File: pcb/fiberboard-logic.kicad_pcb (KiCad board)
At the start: 2 copper layers, 172 x 98 mm, 59 parts, among them J1 VIN, J3 FOOT, J4 NPN, J5 RLY1, J6 RLY2, J7 SOL, J8 RS485, J9 OLED, K1 G6KU-2F-Y, K2 G6KU-2F-Y, Q12 AO4407A, Q3 2N3904, Q4 2N3904, Q5 AO3400A, U1 ESP32-DevKitC, U2 XL1509-5.0, U3 AMS1117-3.3, U5 PC817, U6 PC817, U7 MAX485E

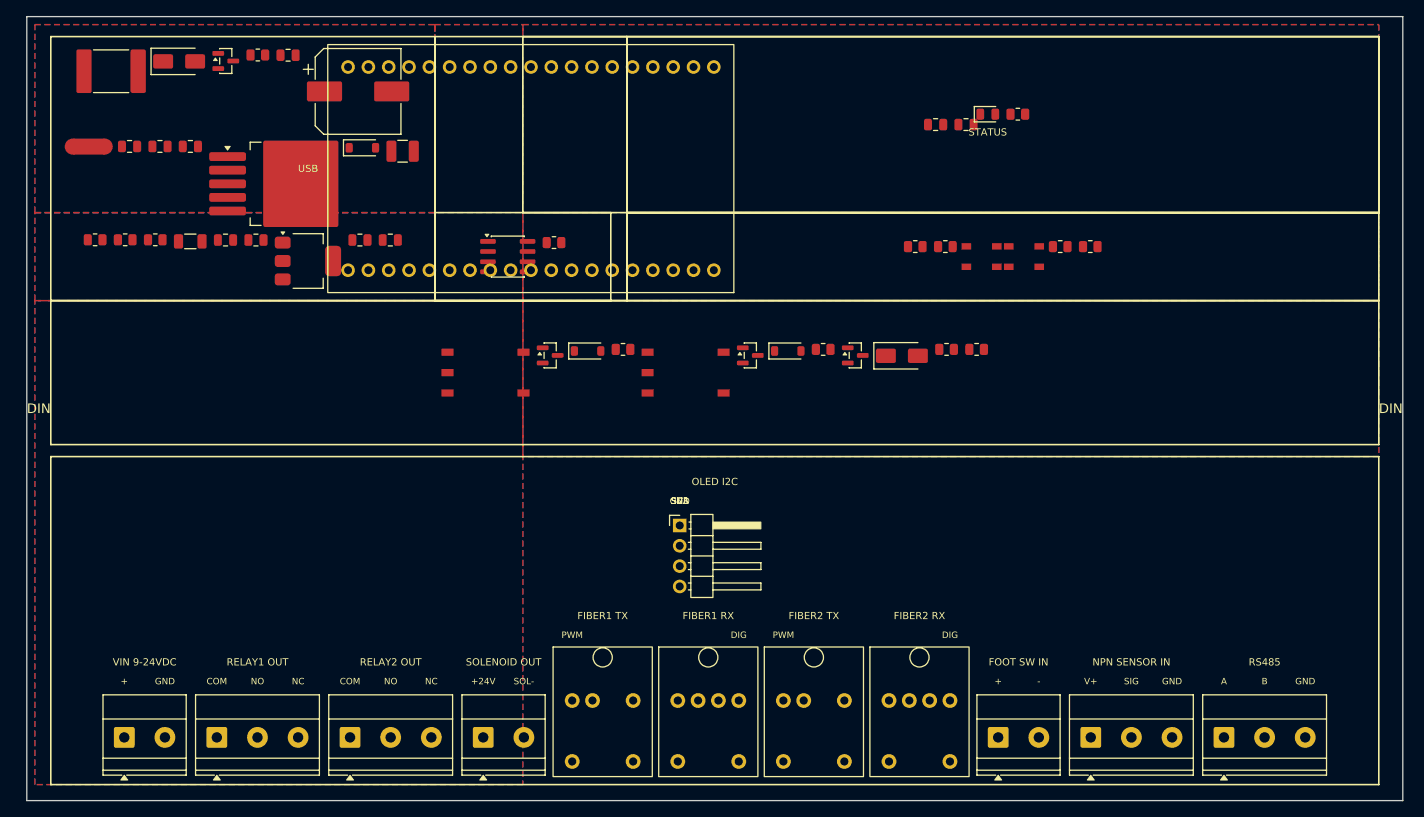
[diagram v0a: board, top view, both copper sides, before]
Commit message: thêm các linh kiện bảo vệ nguồn và sửa layout để lắp vào hộp PLC 45x90x40mm 2 hàng giắc
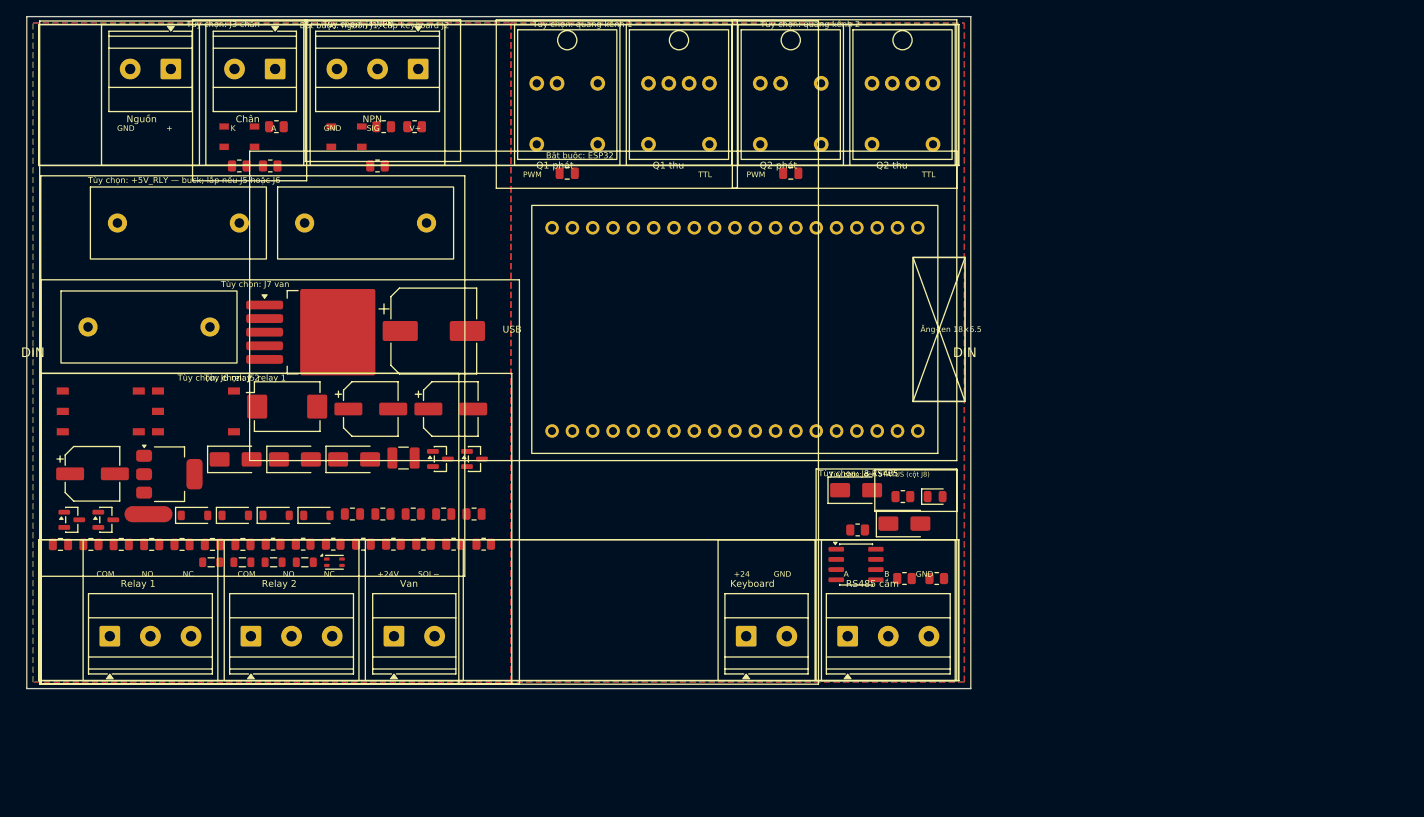
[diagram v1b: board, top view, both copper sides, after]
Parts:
- removed J9: OLED, Connector_PinHeader_2.54mm:PinHeader_1x04_P2.54mm_Horizontal
- added C19: 10uF, Capacitor_SMD:C_0805_2012Metric, F.Cu at (40.7, 62.2)
- added C21: 100nF, Capacitor_SMD:C_0805_2012Metric, F.Cu at (23.2, 66.0)
- added C22: 220uF, Capacitor_SMD:CP_Elec_6.3x5.4, F.Cu at (53.0, 49.0)
- added C23: 100nF, Capacitor_SMD:C_0805_2012Metric, F.Cu at (52.1, 62.2)
- added C24: 220uF, Capacitor_SMD:CP_Elec_6.3x5.4, F.Cu at (8.21, 57.1)
- added C25: 100nF, Capacitor_SMD:C_0805_2012Metric, F.Cu at (27.0, 66.0)
- added D10: SMAJ5.0A, Diode_SMD:D_SMA, F.Cu at (103.7, 59.2)
- added D11: SMAJ5.0A, Diode_SMD:D_SMA, F.Cu at (33.5, 55.4)
- added D12: SMAJ5.0A, Diode_SMD:D_SMA, F.Cu at (40.9, 55.4)
- added D9: SMAJ5.0A, Diode_SMD:D_SMA, F.Cu at (109.7, 63.4)
- added F2: 5x20 F0.5A, Fiberboard:Fuseholder_5x20mm_Horizontal, F.Cu at (42.4, 25.8)
- added F3: 5x20 F0.25A, Fiberboard:Fuseholder_5x20mm_Horizontal, F.Cu at (15.3, 38.8)
- added FB1: BLM21PG121, Inductor_SMD:L_0805_2012Metric, F.Cu at (30.9, 68.2)
- added FB2: BLM21PG121, Inductor_SMD:L_0805_2012Metric, F.Cu at (26.9, 68.2)
- added FB3: BLM21PG121, Inductor_SMD:L_0805_2012Metric, F.Cu at (23.1, 68.2)
- added FB4: BLM21PG121, Inductor_SMD:L_0805_2012Metric, F.Cu at (34.8, 68.2)
- added J2: KB24, Fiberboard:Terminal_2EDG5.08-1x02_P5.08mm_Horizontal, F.Cu at (89.9, 77.5)
- added L2: ACM2012, Inductor_SMD:L_CommonModeChoke_Coilank_ACM2012, F.Cu at (38.5, 68.2)
- added R18: 10R, Resistor_SMD:R_0805_2012Metric, F.Cu at (113.7, 70.2)
- added R19: 10R, Resistor_SMD:R_0805_2012Metric, F.Cu at (103.9, 64.2)
- added R20: 100k, Resistor_SMD:R_0805_2012Metric, F.Cu at (30.4, 18.7)
- added R21: 100k, Resistor_SMD:R_0805_2012Metric, F.Cu at (43.8, 18.7)
- added RV1: MOV-26V, Varistor:Varistor_Panasonic_VF, F.Cu at (32.5, 48.8)
- C2: value 100uF -> 220uF; footprint Capacitor_SMD:C_1206_3216Metric -> Capacitor_SMD:CP_Elec_6.3x5.4
- C4: value 470uF -> 1000uF; footprint Capacitor_SMD:CP_Elec_10x10.5 -> Capacitor_SMD:CP_Elec_10x12.5
- D3, D4: value 1N4148 -> SS34
- D5: footprint Diode_SMD:D_SMA -> Diode_SMD:D_SOD-123
- F1: value MF-MSMF350 -> 5x20 F4A; footprint Fuse:Fuse_2920_7451Metric -> Fiberboard:Fuseholder_5x20mm_Horizontal
- J1, J3, J7: footprint TerminalBlock_Phoenix:TerminalBlock_Phoenix_MKDS-1,5-2-5.08_1x02_P5.08mm_Horizontal -> Fiberboard:Terminal_2EDG5.08-1x02_P5.08mm_Horizontal
- J4, J5, J6: footprint TerminalBlock_Phoenix:TerminalBlock_Phoenix_MKDS-1,5-3-5.08_1x03_P5.08mm_Horizontal -> Fiberboard:Terminal_2EDG5.08-1x03_P5.08mm_Horizontal
- J8: value RS485 -> RS485-2EDG3P; footprint TerminalBlock_Phoenix:TerminalBlock_Phoenix_MKDS-1,5-3-5.08_1x03_P5.08mm_Horizontal -> Fiberboard:Terminal_2EDG5.08-1x03_P5.08mm_Horizontal
- R13: value 100R -> 100
- R15: value 120R -> 100
- U1: value ESP32-DevKitC -> ESP32-DevKitC-32E
- moved J3 123.1 mm to (31.0, 6.55), turned to 180 degrees
- moved J4 118.5 mm to (48.9, 6.55), turned to 180 degrees
- moved R9 103.1 mm to (26.6, 18.7)
- moved Q5 95.9 mm to (9.88, 62.9)
- moved U5 94.0 mm to (26.6, 15.0)
- moved Q4 87.3 mm to (5.62, 62.9)
- moved U6 86.0 mm to (40.0, 15.0)
- moved R10 85.8 mm to (48.5, 13.8)
- moved J1 83.8 mm to (18.0, 6.55), turned to 180 degrees
- moved R7 81.2 mm to (31.2, 13.8)
- moved F1T 77.3 mm to (67.6, 12.2)
- moved F1R 77.2 mm to (81.5, 12.2)
- moved F2T 77.2 mm to (95.5, 12.2)
- moved F2R 77.2 mm to (109.5, 12.2)
- moved D5 75.8 mm to (36.3, 62.4)
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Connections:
- C18 pad 1: +3V3 -> +3V3_REG
- C2 pad 1: +5V -> +5V_RAW
- C3 pad 1: +3V3 -> +3V3_REG
- C5 pad 1: +5V -> +5V_RAW
- D3 pad 1: +5V -> +5V_RLY
- D4 pad 1: +5V -> +5V_RLY
- D5 pad 1: +24V -> +24V_SOL
- F1 pad 2: VIN_FUSE -> VIN_CM_IN
- J1 pad 2: GND_PWR -> VIN_CM_RET
- J7 pad 1: +24V -> +24V_SOL
- J8 pad 1: RS485_A -> RS485_A_BUS
- J8 pad 2: RS485_B -> RS485_B_BUS
- K1 pad 1: +5V -> +5V_RLY
- K2 pad 1: +5V -> +5V_RLY
- L1 pad 2: +5V -> +5V_RAW
- NT1 pad 2: GND -> GND_SPLICE
- R15 pad 1: RS485_A -> RS485_A_BUS
- R15 pad 2: RS485_B -> RS485_B_BUS
- U1 pad 13: GND -> (no net)
- U1 pad 14: (no net) -> GND
- U3 pad 2: +3V3 -> +3V3_REG
- U6 pad 2: GND -> GND_PWR
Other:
- board size 172 x 98 mm -> 118 x 84 mm
- board text added: "+24"
- board text added: "Bắt buộc: ESP32"
- board text added: "Bắt buộc: nguồn J1, cấp keyboard J2"
- board text added: "Chân"
- board text added: "K"
- board text added: "Keyboard"
- board text added: "NPN"
- board text added: "Nguồn"
- board text added: "Q1 phát"
- board text added: "Q1 thu"
- board text added: "Q2 phát"
- board text added: "Q2 thu"
- board text added: "RS485 cắm"
- board text added: "Relay 1"
- board text added: "Relay 2"
- board text added: "SOL−"
- board text added: "TTL"
- board text added: "Tùy chọn: +5V_RLY — buck; lắp nếu J5 hoặc J6"
- board text added: "Tùy chọn: J3 chân"
- board text added: "Tùy chọn: J4 NPN"
- board text added: "Tùy chọn: J5 relay 1"
- board text added: "Tùy chọn: J6 relay 2"
- board text added: "Tùy chọn: J7 van"
- board text added: "Tùy chọn: J8 RS485"
- board text added: "Tùy chọn: quang kênh 1"
- board text added: "Tùy chọn: quang kênh 2"
- board text added: "Tùy chọn: đèn STATUS (cột J8)"
- board text added: "Van"
- board text added: "Ăng-ten 18×6.5"
- board text removed: "-"
- board text removed: "3V3"
- board text removed: "DIG"
- board text removed: "FIBER1 RX"
- board text removed: "FIBER1 TX"
- board text removed: "FIBER2 RX"
- board text removed: "FIBER2 TX"
- board text removed: "FOOT SW IN"
- board text removed: "NPN SENSOR IN"
- board text removed: "OLED I2C"
- board text removed: "RELAY1 OUT"
- board text removed: "RELAY2 OUT"
- board text removed: "RS485"
- board text removed: "SCL"
- board text removed: "SDA"
- board text removed: "SOL-"
- board text removed: "SOLENOID OUT"
- board text removed: "STATUS"
- board text removed: "VIN 9-24VDC"

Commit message: chia vùng linh kiện để sắp xếp và tránh linh kiện quá dày
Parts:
- removed F2: 5x20 F0.5A, Fiberboard:Fuseholder_5x20mm_Horizontal
- removed F3: 5x20 F0.25A, Fiberboard:Fuseholder_5x20mm_Horizontal
- added C26: 220uF, Capacitor_SMD:CP_Elec_6.3x5.4, F.Cu at (50.3, 67.7)
- added C27: 100nF, Capacitor_SMD:C_0805_2012Metric, F.Cu at (52.8, 62.2)
- added D13: VIN, LED_SMD:LED_0805_2012Metric, F.Cu at (8.07, 13.8)
- added D14: KB24, LED_SMD:LED_0805_2012Metric, F.Cu at (85.9, 70.2)
- added D15: FOOT, LED_SMD:LED_0805_2012Metric, F.Cu at (18.3, 13.8)
- added D16: NPN, LED_SMD:LED_0805_2012Metric, F.Cu at (39.1, 13.8)
- added D17: RLY1, LED_SMD:LED_0805_2012Metric, F.Cu at (25.5, 62.2)
- added D18: RLY2, LED_SMD:LED_0805_2012Metric, F.Cu at (56.6, 62.2)
- added D19: VAN, LED_SMD:LED_0805_2012Metric, F.Cu at (73.7, 65.0)
- added D20: 485, LED_SMD:LED_0805_2012Metric, F.Cu at (98.4, 70.2)
- added D21: TX1, LED_SMD:LED_0805_2012Metric, F.Cu at (63.7, 19.6)
- added D22: RX1, LED_SMD:LED_0805_2012Metric, F.Cu at (79.6, 19.6)
- added D23: TX2, LED_SMD:LED_0805_2012Metric, F.Cu at (91.6, 19.6)
- added D24: RX2, LED_SMD:LED_0805_2012Metric, F.Cu at (107.6, 19.6)
- added D25: 5V, LED_SMD:LED_0805_2012Metric, F.Cu at (49.2, 39.5)
- added D26: SMAJ5.0A, Diode_SMD:D_SMA, F.Cu at (59.0, 69.5)
- added D27: 24V, LED_SMD:LED_0805_2012Metric, F.Cu at (27.8, 44.9)
- added FB5: BLM21PG121, Inductor_SMD:L_0805_2012Metric, F.Cu at (48.9, 62.3)
- added R22: 10k, Resistor_SMD:R_0805_2012Metric, F.Cu at (8.07, 19.6)
- added R23: 10k, Resistor_SMD:R_0805_2012Metric, F.Cu at (85.9, 65.9)
- added R24: 1k, Resistor_SMD:R_0805_2012Metric, F.Cu at (18.3, 18.1)
- added R25: 1k, Resistor_SMD:R_0805_2012Metric, F.Cu at (39.1, 18.1)
- added R26: 1k, Resistor_SMD:R_0805_2012Metric, F.Cu at (25.5, 57.9)
- added R27: 1k, Resistor_SMD:R_0805_2012Metric, F.Cu at (56.6, 57.9)
- added R28: 10k, Resistor_SMD:R_0805_2012Metric, F.Cu at (73.7, 60.7)
- added R29: 1k, Resistor_SMD:R_0805_2012Metric, F.Cu at (96.2, 63.7)
- added R30: 1k, Resistor_SMD:R_0805_2012Metric, F.Cu at (63.7, 22.1)
- added R31: 1k, Resistor_SMD:R_0805_2012Metric, F.Cu at (79.6, 22.1)
- added R32: 1k, Resistor_SMD:R_0805_2012Metric, F.Cu at (91.6, 22.1)
- added R33: 1k, Resistor_SMD:R_0805_2012Metric, F.Cu at (107.6, 22.1)
- added R34: 1k, Resistor_SMD:R_0805_2012Metric, F.Cu at (49.2, 41.6)
- added R39: 10k, Resistor_SMD:R_0805_2012Metric, F.Cu at (27.8, 47.0)
- added R40: 1k, Resistor_SMD:R_0805_2012Metric, F.Cu at (94.6, 47.3)
- added R41: 1k, Resistor_SMD:R_0805_2012Metric, F.Cu at (90.5, 47.3)
- added R42: 1k, Resistor_SMD:R_0805_2012Metric, F.Cu at (77.8, 27.8)
- added R43: 1k, Resistor_SMD:R_0805_2012Metric, F.Cu at (71.7, 27.8)
- added R44: 1k, Resistor_SMD:R_0805_2012Metric, F.Cu at (106.8, 27.8)
- added R45: 1k, Resistor_SMD:R_0805_2012Metric, F.Cu at (81.9, 27.8)
- D6: value STATUS -> 3V3
- moved D6 68.2 mm to (46.5, 47.1)
- moved R16 63.9 mm to (46.5, 49.2)
- moved R20 62.9 mm to (86.5, 47.3)
- moved Q5 60.3 mm to (69.8, 69.6)
- moved C17 56.7 mm to (39.7, 21.8)
- moved R21 48.1 mm to (82.4, 47.3)
- moved Q12 47.8 mm to (5.45, 43.4)
- moved L2 47.5 mm to (28.7, 21.7)
- moved Q3 46.3 mm to (10.0, 61.4)
- moved C16 45.1 mm to (35.8, 21.8)
- moved C19 44.7 mm to (5.03, 35.3)
- moved C15 44.3 mm to (9.28, 35.3)
- moved C5 44.3 mm to (49.4, 37.2)
- moved C7 44.1 mm to (46.7, 44.8)
- moved FB2 40.8 mm to (53.3, 37.1)
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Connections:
- net FOOT_LED renamed FOOT_AN
- net NPN_LED renamed NPN_AN
- net STAT_LED renamed P3V3_AN
- C24 pad 1: +5V_RLY -> +5V_RLY1
- C25 pad 1: +5V_RLY -> +5V_RLY1
- D12 pad 1: +5V_RLY -> +5V_RLY1
- D3 pad 1: +5V_RLY -> +5V_RLY1
- D4 pad 1: +5V_RLY -> +5V_RLY2
- D5 pad 1: +24V_SOL -> +24V
- F1R pad 1: FIBER1_DIG -> FIBER1_RX
- F1T pad 4: FIBER1_PWM -> FIBER1_TX
- F2R pad 1: FIBER2_DIG -> FIBER2_RX
- F2T pad 4: FIBER2_PWM -> FIBER2_TX
- FB4 pad 2: +5V_RLY -> +5V_RLY1
- J7 pad 1: +24V_SOL -> +24V
- K1 pad 1: +5V_RLY -> +5V_RLY1
- K2 pad 1: +5V_RLY -> +5V_RLY2
- U7 pad 1: RS485_RX -> RS485_RO
- U7 pad 4: RS485_TX -> RS485_DI
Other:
- board text added: "24V"
- board text added: "3V3"
- board text added: "5V"
- board text added: "Bắt buộc: J1 nguồn vào, J2 cấp bàn phím"
- board text added: "Bắt buộc: MCU"
- board text added: "Bắt buộc: buck 5 V / LDO 3,3 V"
- board text added: "Bắt buộc: bảo vệ 24 V"
- board text added: "C 1000uF"
- board text added: "C 100nF"
- board text added: "C 10uF"
- board text added: "C 220uF"
- board text added: "C 22uF"
- board text added: "MOS"
- board text added: "R 100"
- board text added: "R 100k"
- board text added: "R 10R"
- board text added: "R 10k"
- board text added: "R 1k"
- board text added: "R 3k"
- board text removed: "Bắt buộc: ESP32"
- board text removed: "Bắt buộc: nguồn J1, cấp keyboard J2"
- board text removed: "Tùy chọn: +5V_RLY — buck; lắp nếu J5 hoặc J6"
- board text removed: "Tùy chọn: đèn STATUS (cột J8)"
- board text removed: "USB"
- board text removed: "Ăng-ten 18×6.5"
